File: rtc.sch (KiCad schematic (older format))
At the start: 3 parts, among them U2 DS3231M

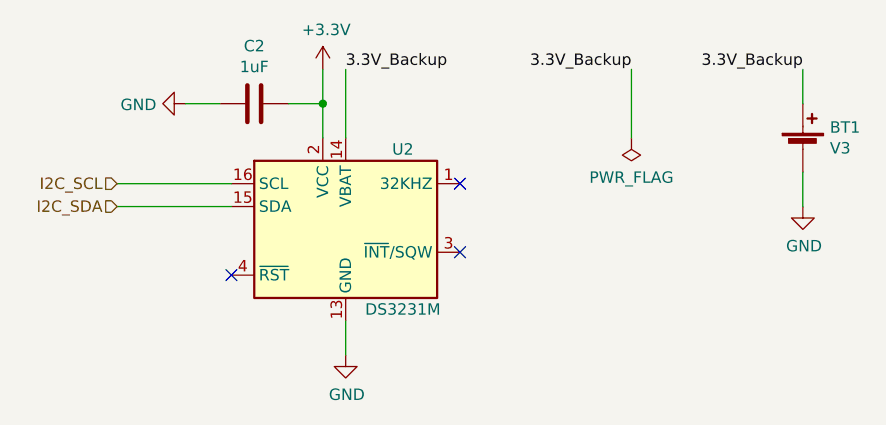
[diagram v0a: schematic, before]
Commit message: Added MFN, MPN, VN and VPN fields for all symbols
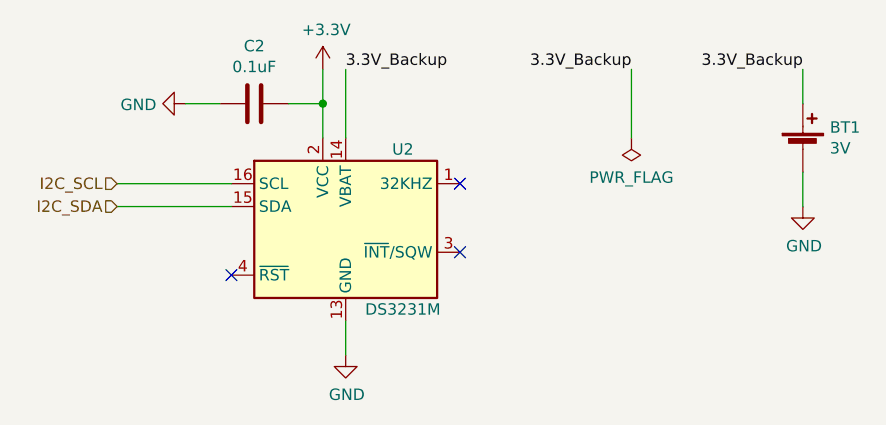
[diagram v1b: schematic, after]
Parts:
- BT1: value V3 -> 3V; MFN (none) -> Keystone Electronics; MPN (none) -> 3000; VN (none) -> Digikey; VPN (none) -> 36-3000-ND
- C2: value 1uF -> 0.1uF; MFN (none) -> Generic; MPN (none) -> Generic; VN (none) -> Digikey; VPN (none) -> 311-1777-1-ND
- U2: MFN (none) -> Maxim Integrated; MPN (none) -> DS3231SN#T&R; VN (none) -> Digikey; VPN (none) -> DS3231SN#T&RCT-ND
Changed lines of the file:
@@
 AR Path="/5E624F1D/5E62F10F" Ref="C2"  Part="1"
 F 0 "C2" V 5098 3500 50  0000 C CNN
-F 1 "1uF" V 5189 3500 50  0000 C CNN
+F 1 "0.1uF" V 5189 3500 50  0000 C CNN
 F 2 "Capacitor_SMD:C_0603_1608Metric_Pad1.05x0.95mm_HandSolder" H 5388 3350 50  0001 C CNN
 F 3 "~" H 5350 3500 50  0001 C CNN
+F 4 "Digikey" H 5350 3500 50  0001 C CNN "VN"
+F 5 "Generic" H 5350 3500 50  0001 C CNN "MFN"
+F 6 "Generic" H 5350 3500 50  0001 C CNN "MPN"
+F 7 "311-1777-1-ND" H 5350 3500 50  0001 C CNN "VPN"
 	1    5350 3500
 	0    1    1    0
@@
 F 2 "Package_SO:SOIC-16W_7.5x10.3mm_P1.27mm" H 5750 3450 50  0001 C CNN
 F 3 "http://datasheets.maximintegrated.com/en/ds/DS3231.pdf" H 6020 4100 50  0001 C CNN
+F 4 "Digikey" H 5750 4050 50  0001 C CNN "VN"
+F 5 "Maxim Integrated" H 5750 4050 50  0001 C CNN "MFN"
+F 6 "DS3231SN#T&R" H 5750 4050 50  0001 C CNN "MPN"
+F 7 "DS3231SN#T&RCT-ND" H 5750 4050 50  0001 C CNN "VPN"
 	1    5750 4050
 	1    0    0    -1
@@
 P 7750 3700
 F 0 "BT1" H 7868 3796 50  0000 L CNN
-F 1 "V3" H 7868 3705 50  0000 L CNN
+F 1 "3V" H 7868 3705 50  0000 L CNN
 F 2 "Battery:BatteryHolder_Keystone_3000_1x12mm" V 7750 3760 50  0001 C CNN
-F 3 "~" V 7750 3760 50  0001 C CNN
+F 3 "https://www.keyelco.com/userAssets/file/M65p9.pdf" V 7750 3760 50  0001 C CNN
+F 4 "Digikey" H 7750 3700 50  0001 C CNN "VN"
+F 5 "Keystone Electronics" H 7750 3700 50  0001 C CNN "MFN"
+F 6 "3000" H 7750 3700 50  0001 C CNN "MPN"
+F 7 "36-3000-ND" H 7750 3700 50  0001 C CNN "VPN"
 	1    7750 3700
 	1    0    0    -1
